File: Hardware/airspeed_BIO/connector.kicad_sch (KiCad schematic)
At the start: 0 parts

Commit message: power end didn't set I limit
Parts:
- added C4: 4.7n, Capacitor_SMD:C_0402_1005Metric, symbol Device:C_Small
- added C45: 1u, Capacitor_SMD:C_0402_1005Metric, symbol Device:C_Small
- added C47: 0.1u, Capacitor_SMD:C_0402_1005Metric, symbol Device:C_Small
- added J1: USB_C_Receptacle_USB2.0_16P, TTR:USB_C_Receptacle_WE_632723300011_hand, symbol Connector:USB_C_Receptacle_USB2.0_16P
- added R10, R11: 5.1k, Resistor_SMD:R_0402_1005Metric, symbol Device:R_Small
- added R9: 1M, Resistor_SMD:R_0402_1005Metric, symbol Device:R_Small
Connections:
- new net: C4.1, J1.S1 (SHIELD), R9.1
- new net: J1.B5 (CC2), R11.2
- new net: J1.A5 (CC1), R10.2
- new net GND: C4.2, C45.2, C47.2, J1.A1 (GND), J1.A12 (GND), J1.B1 (GND), J1.B12 (GND), R10.1, R11.1, R9.2
- new net USB.D+: J1.A6 (D+), J1.B6 (D+)
- new net USB.D-: J1.A7 (D-), J1.B7 (D-)
- new net USB.VBUS: C45.1, C47.1, J1.A4 (VBUS), J1.A9 (VBUS), J1.B4 (VBUS), J1.B9 (VBUS)
- no-connect marks 0 -> 2
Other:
- note added: "get 5V"

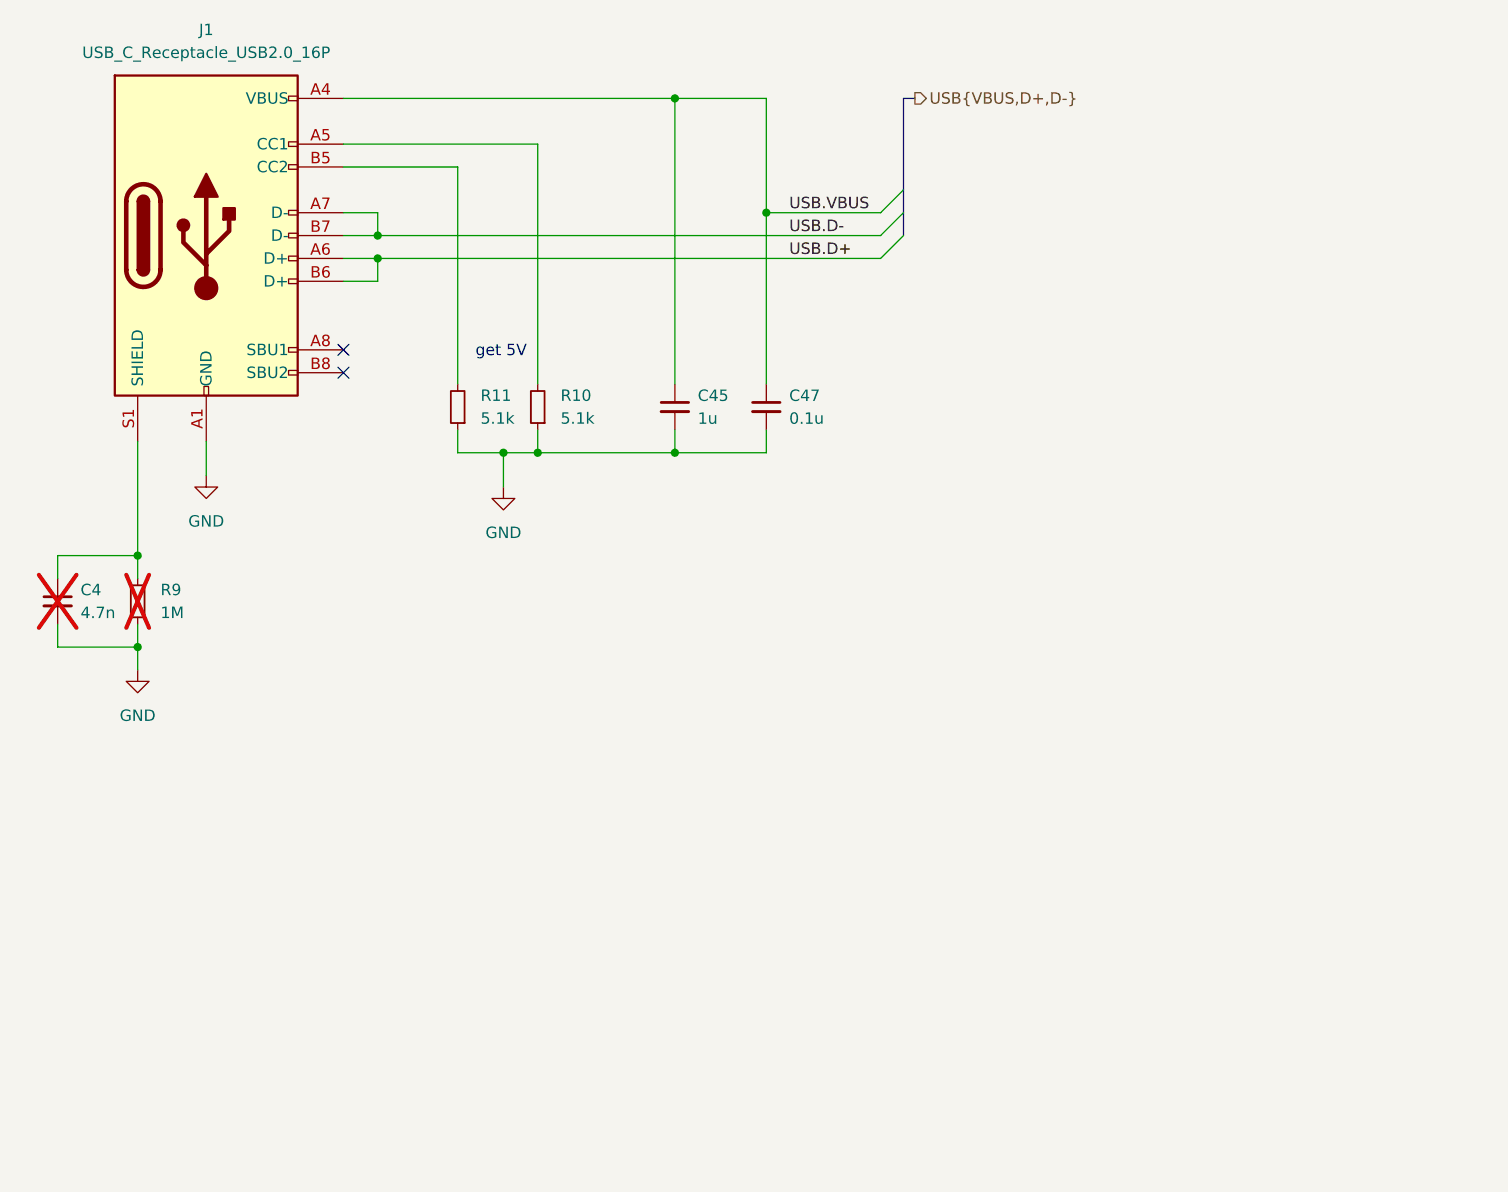
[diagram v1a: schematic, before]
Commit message: add mcu audio
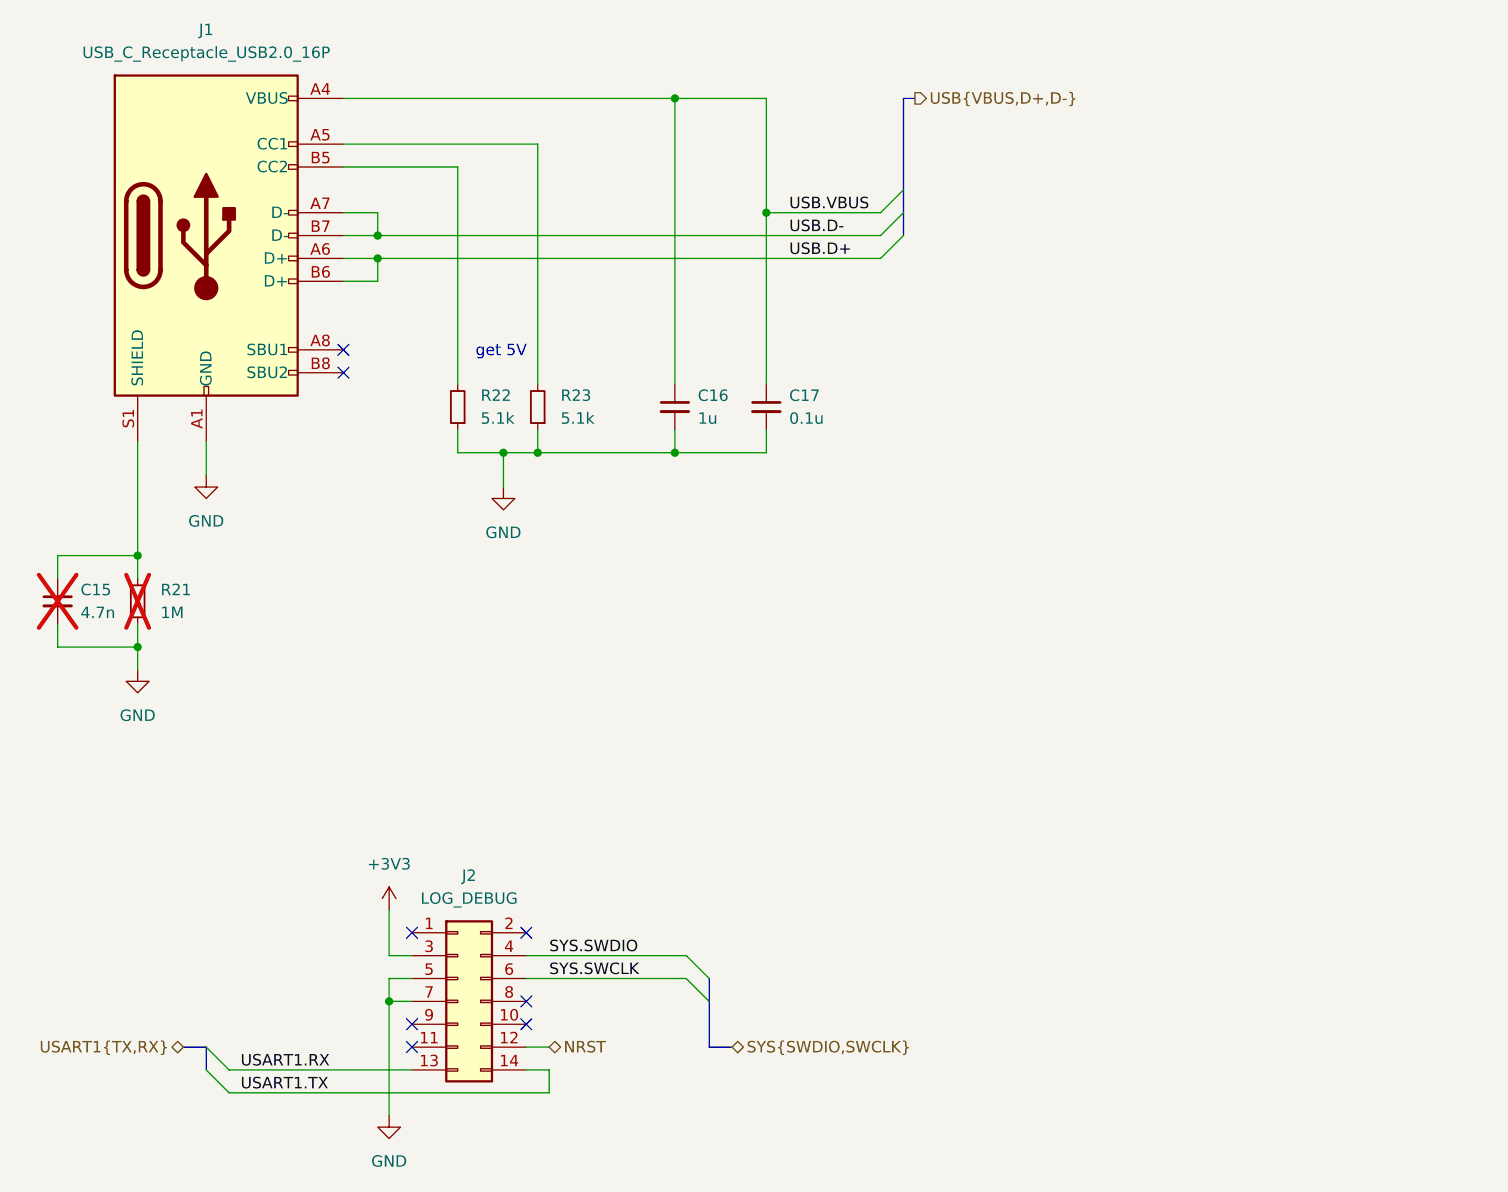
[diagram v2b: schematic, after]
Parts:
- added J2: LOG_DEBUG, TTR:62731420621, symbol Connector_Generic:Conn_02x07_Odd_Even
- renumbered C4 to C15, C45 to C16, C47 to C17, R9 to R21, R11 to R22, R10 to R23
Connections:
- net GND: now also J2.5 (Pin_5), J2.7 (Pin_7)
- new net +3V3: J2.3 (Pin_3)
- new net NRST: J2.12 (Pin_12)
- new net SYS.SWCLK: J2.6 (Pin_6)
- new net SYS.SWDIO: J2.4 (Pin_4)
- new net USART1.RX: J2.13 (Pin_13)
- new net USART1.TX: J2.14 (Pin_14)
- no-connect marks 2 -> 8
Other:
- company: (none) -> Taipei Tech Racing

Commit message: set Ilimit and set footprint
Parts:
- added J4: BATT, Connector_JST:JST_XH_S2B-XH-A-1_1x02_P2.50mm_Horizontal, symbol Connector_Generic:Conn_01x02
- added R28, R29: 2.1K, Resistor_SMD:R_0603_1608Metric, symbol Device:R_Small
- added SW3: SW_SPDT, TTR:switch_450301014042, symbol Switch:SW_SPDT
- C15, C16, C17: footprint Capacitor_SMD:C_0402_1005Metric -> Capacitor_SMD:C_0603_1608Metric
- R21, R22, R23: footprint Resistor_SMD:R_0402_1005Metric -> Resistor_SMD:R_0603_1608Metric
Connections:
- net GND: now also J4.1 (Pin_1), R29.2
- new net: R28.2, SW3.1 (A)
- new net: R29.1, SW3.3 (C)
- new net BATT: J4.2 (Pin_2)
- new net EN_power: SW3.2 (B)
- new net VCCmp: R28.1

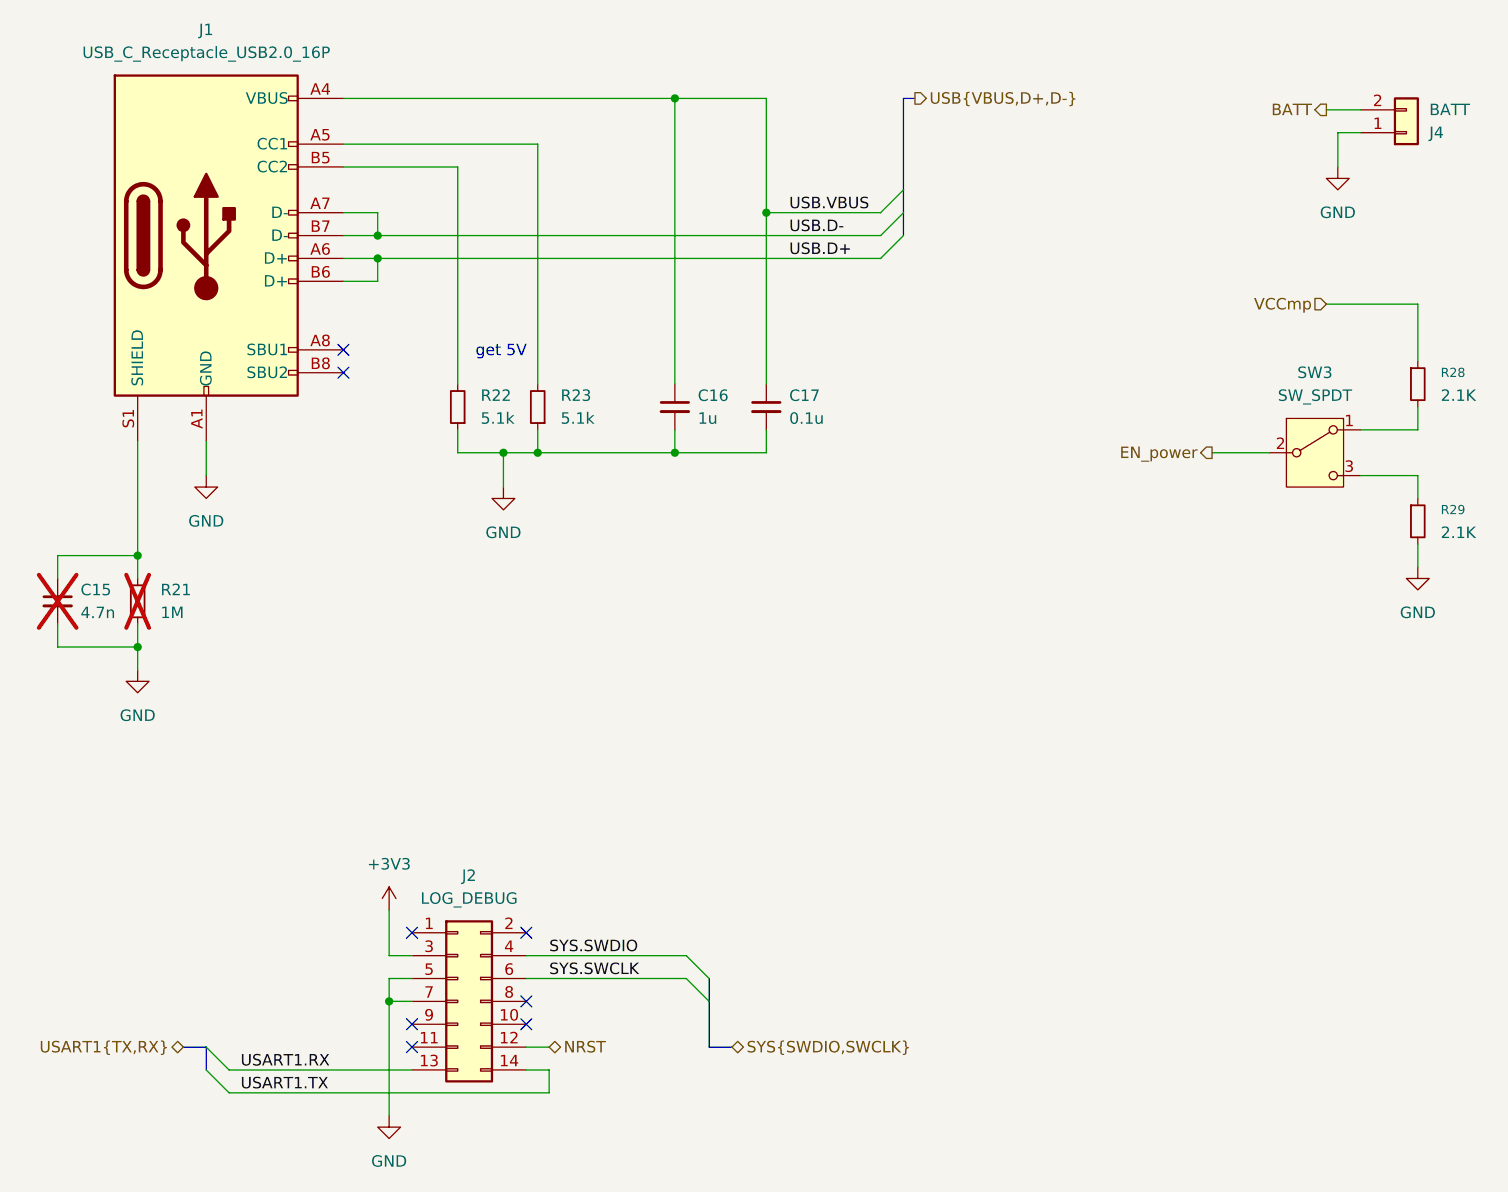
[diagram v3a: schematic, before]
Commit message: layout and fix Schematic
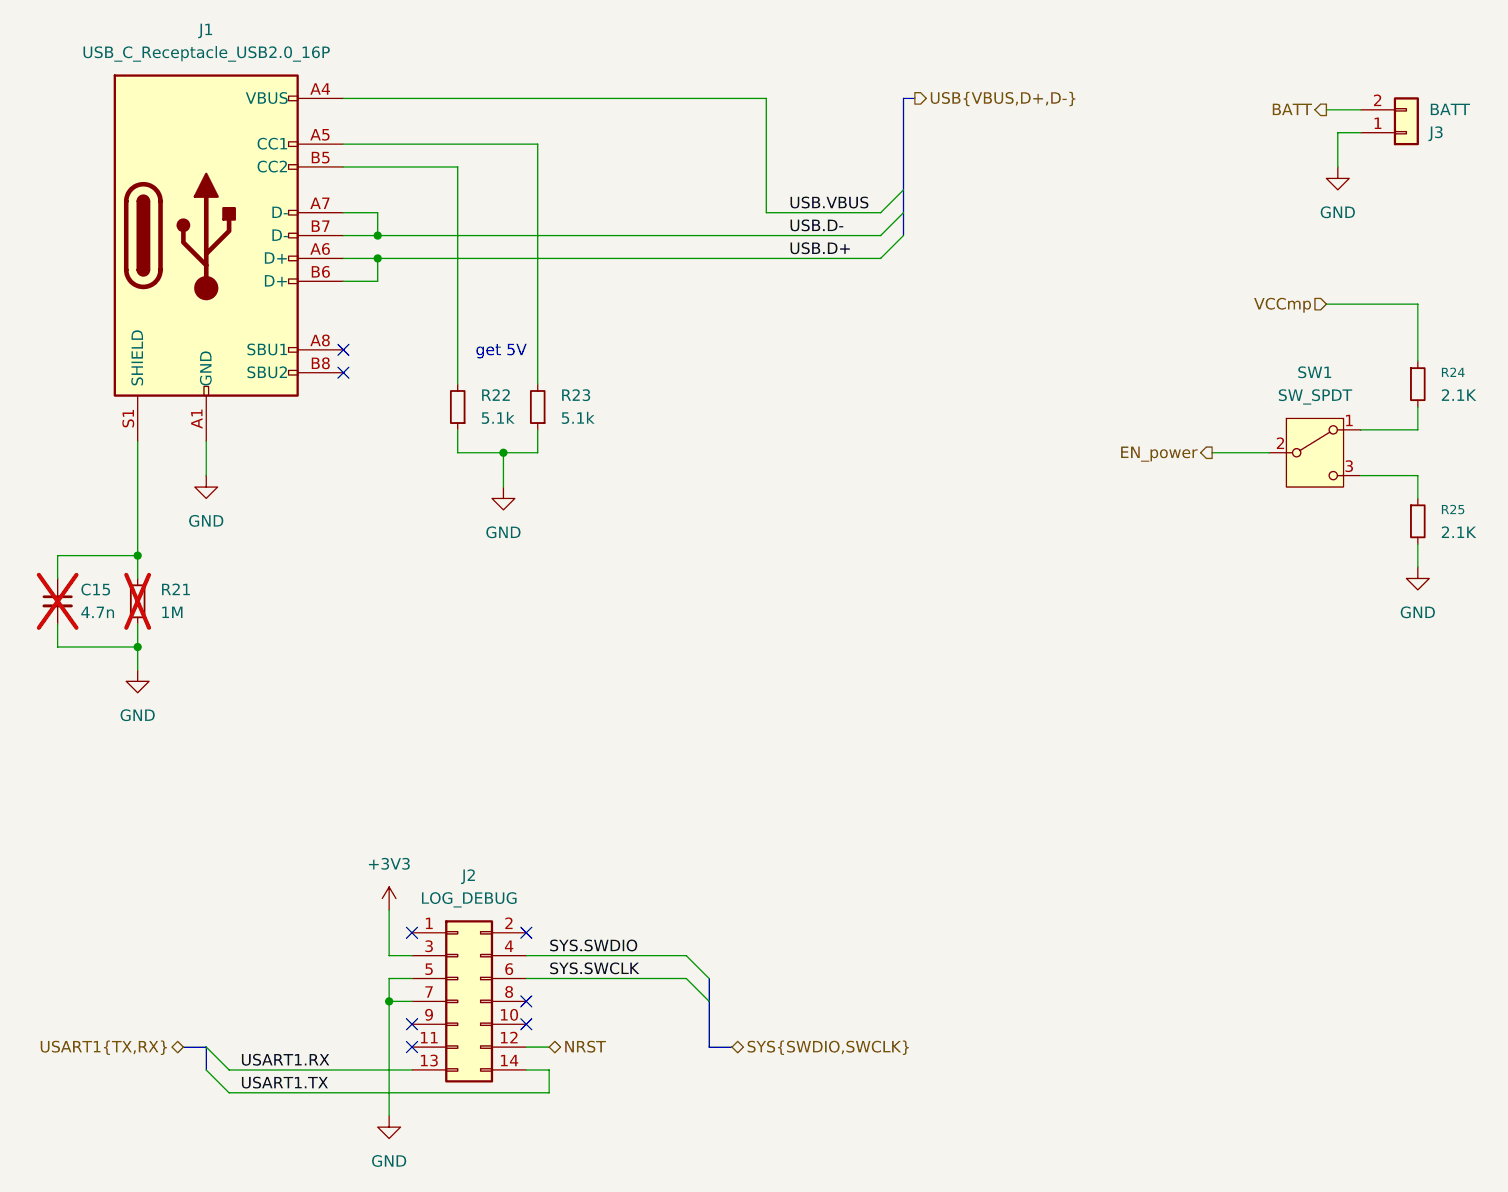
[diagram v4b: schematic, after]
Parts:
- removed C16: 1u, Capacitor_SMD:C_0603_1608Metric, symbol Device:C_Small
- removed C17: 0.1u, Capacitor_SMD:C_0603_1608Metric, symbol Device:C_Small
- renumbered J4 to J3, R28 to R24, R29 to R25, SW3 to SW1

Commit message: layoyt end
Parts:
- renumbered C15 to C14
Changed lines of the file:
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@@
 		(dnp yes)
 		(fields_autoplaced yes)
-		(property "Reference" "C15"
+		(property "Reference" "C14"
 			(at 35.56 86.3662 0)
 			(effects
@@
 			(project "airspeed_BIO"
 				(path "/6ddcf4fe-9e51-4114-8222-5fc3f810c12a/679a9433-c527-4736-baca-b3e5544bf971"
-					(reference "C15")
+					(reference "C14")
 					(unit 1)
 				)
